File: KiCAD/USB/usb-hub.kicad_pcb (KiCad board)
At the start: 2 copper layers, 15 x 20 mm, 1 part, among them J1 046809610110846+ Male

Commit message: stuffs
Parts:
- added C1: 0.1μF, Capacitor_SMD:C_01005_0402Metric, F.Cu at (144.0, 42.5)
- added C10: 30 pF, Capacitor_SMD:C_01005_0402Metric, F.Cu at (149.2, 50.3)
- added C11: 30 pF, Capacitor_SMD:C_01005_0402Metric, F.Cu at (154.6, 45.4)
- added C2: 0.1μF, Capacitor_SMD:C_01005_0402Metric, F.Cu at (122.5, 41.5)
- added C3: 0.1μF, Capacitor_SMD:C_01005_0402Metric, F.Cu at (122.5, 43.2)
- added C4: 0.1μF, Capacitor_SMD:C_01005_0402Metric, F.Cu at (122.5, 44.8)
- added C5: 0.1μF, Capacitor_SMD:C_01005_0402Metric, F.Cu at (122.5, 46.5)
- added C6: 10μF, Capacitor_SMD:C_01005_0402Metric, F.Cu at (143.2, 38.5)
- added C8: 10μF, Capacitor_SMD:C_01005_0402Metric, F.Cu at (122.5, 48.1)
- added C9: 10μF, Capacitor_SMD:C_01005_0402Metric, F.Cu at (122.5, 49.8)
- added R1: 649Ω, Resistor_SMD:R_0402_1005Metric, F.Cu at (119.9, 41.7)
- added R2: 10kΩ, Resistor_SMD:R_0402_1005Metric, F.Cu at (151.3, 41.4)
- added R3: 10kΩ, Resistor_SMD:R_0402_1005Metric, F.Cu at (119.9, 43.7)
- added R4: 10kΩ, Resistor_SMD:R_0402_1005Metric, F.Cu at (119.9, 45.7)
- added R5: 10kΩ, Resistor_SMD:R_0402_1005Metric, F.Cu at (119.9, 47.7)
- added R6: 0Ω, Resistor_SMD:R_0402_1005Metric, F.Cu at (119.9, 49.7)
- added R7: 1kΩ, Resistor_SMD:R_0402_1005Metric, F.Cu at (119.9, 51.7)
- added U1: CY7C65634-28LTXC, footprints:QFN-28, F.Cu at (148.0, 44.0)
- added Y1: 12MHz 20pF, Crystal:Crystal_SMD_Abracon_ABM3B-4Pin_5.0x3.2mm, F.Cu at (151.9, 48.0)
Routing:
- net X_IN: track 0.00 -> 8.69 mm
- net X_OUT: track 0.00 -> 8.66 mm
- net GND: track 0.00 -> 5.71 mm, vias 0 -> 3
- net VREG: track 0.00 -> 2.92 mm, vias 0 -> 2
- net Net-(U1-*RESET): track 0.00 -> 1.30 mm
- added copper zone on In1.Cu, net GND
- added copper zone on In2.Cu, net VREG
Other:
- board size 15 x 20 mm -> 16 x 20 mm
- copper layers 2 -> 4

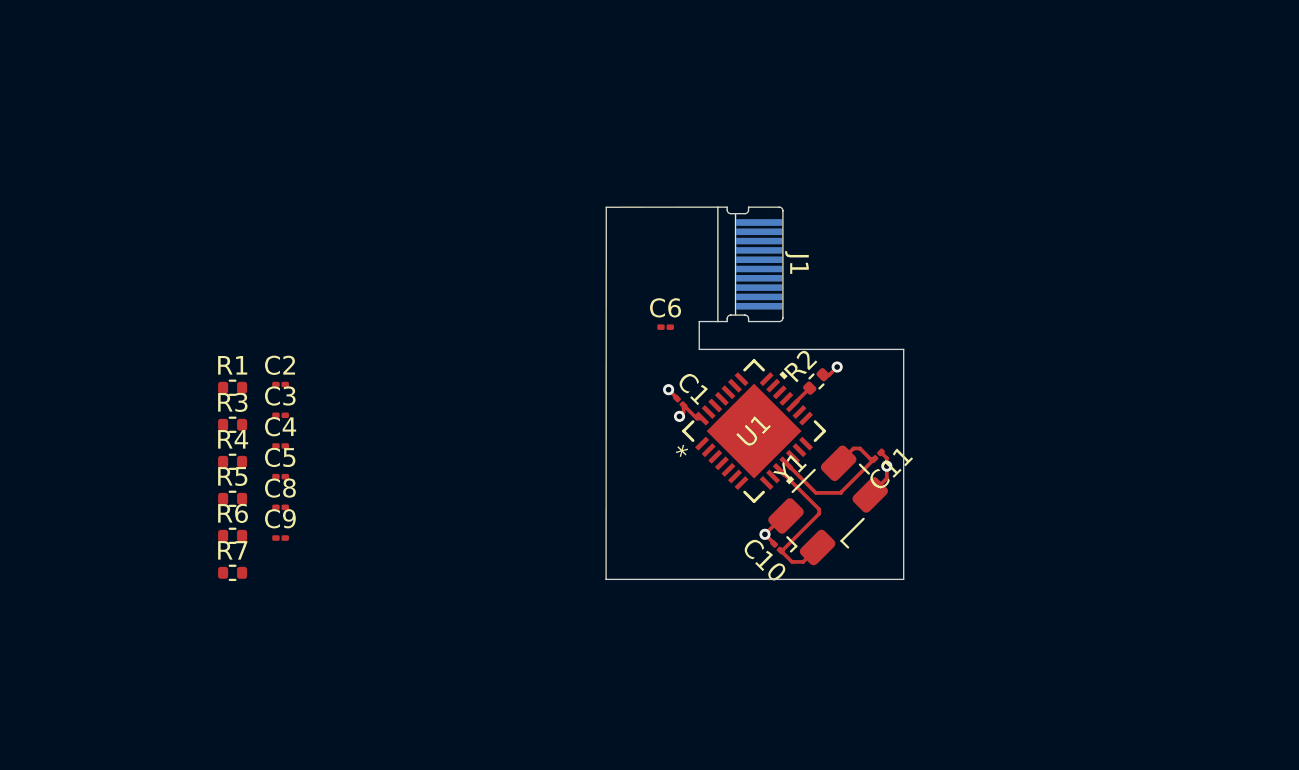
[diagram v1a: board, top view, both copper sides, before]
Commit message: Finish USB hub pcb
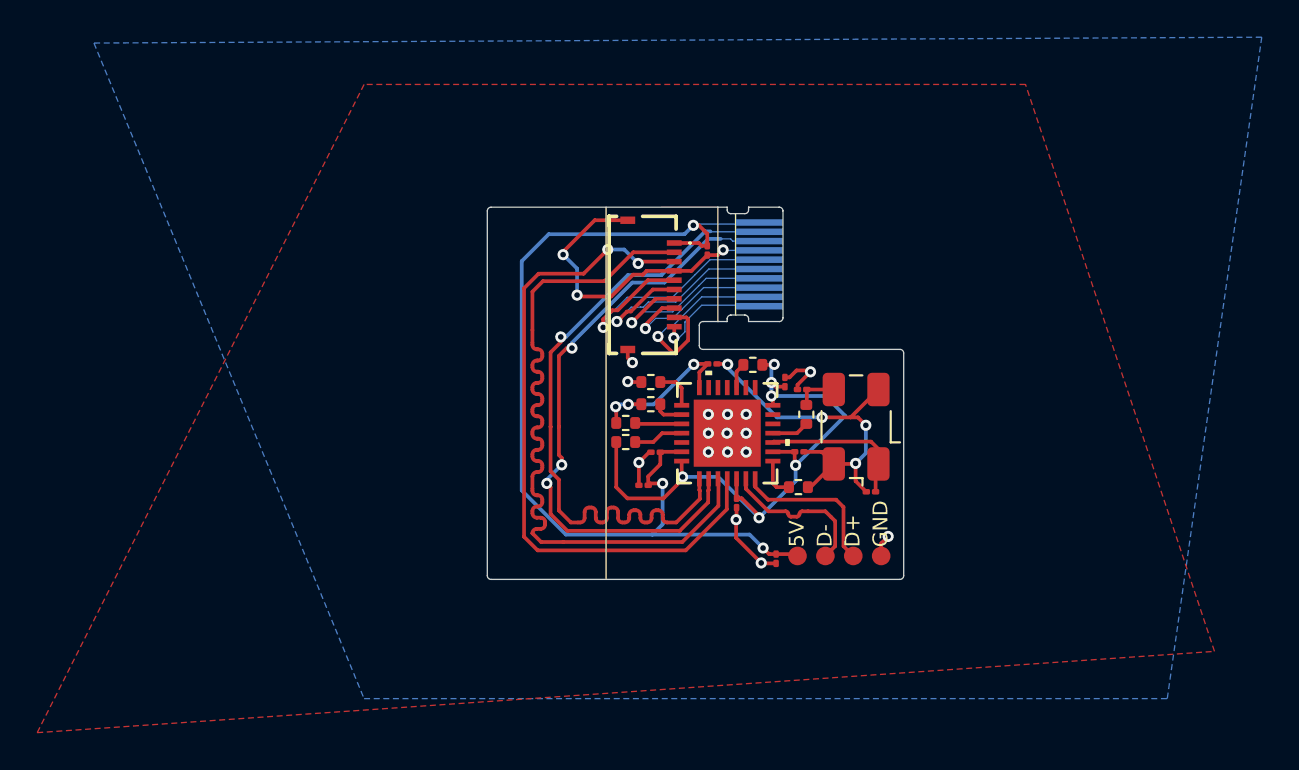
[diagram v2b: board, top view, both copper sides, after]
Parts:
- added J2: 046809610110846+ Female, SamacSys_Parts:046809610110846, F.Cu at (142.0, 36.2)
- added J3: Conn_01x04_Socket, Custom:4 pad, F.Cu at (152.6, 50.8)
- moved R7 32.0 mm to (150.8, 43.1), turned to 90 degrees
- moved R1 30.9 mm to (150.3, 47.0)
- moved C3 28.0 mm to (150.4, 45.1)
- moved C4 27.3 mm to (149.6, 41.4), turned to 90 degrees
- moved C8 26.8 mm to (145.4, 34.3), turned to 90 degrees
- moved C9 26.7 mm to (149.2, 50.9), turned to 90 degrees
- moved C2 25.3 mm to (147.0, 47.9), turned to -90 degrees
- moved R6 24.0 mm to (142.4, 41.4)
- moved R3 22.5 mm to (142.4, 42.6), turned to 180 degrees
- moved R5 21.5 mm to (141.1, 43.6)
- moved R4 21.2 mm to (141.1, 44.6), turned to 180 degrees
- moved C5 20.2 mm to (142.7, 45.2)
- moved C6 8.58 mm to (142.0, 47.0)
- moved C10 5.85 mm to (154.2, 47.3), turned to 180 degrees
- moved C11 5.40 mm to (150.6, 41.8), turned to 0 degrees
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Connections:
- U1 pad 3: USB_KB_N -> USB_FNG_N
- U1 pad 4: USB_KB_P -> USB_FNG_P
- U1 pad 6: USB_FNG_N -> USB_KB_N
- U1 pad 7: USB_FNG_P -> USB_KB_P
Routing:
- net VBUS: track 0.00 -> 52.7 mm, vias 0 -> 3
- net GND: track 5.71 -> 50.4 mm, vias 3 -> 23
- net USB_FNG_N: track 0.00 -> 39.2 mm
- net VREG: track 2.92 -> 41.9 mm, vias 2 -> 9
- net USB_FNG_P: track 0.00 -> 36.4 mm, vias 0 -> 2
- net USB_HOST_N: track 0.00 -> 36.3 mm, vias 0 -> 1
- net USB_HOST_P: track 0.00 -> 33.3 mm, vias 0 -> 3
- net EC_CTRL: track 0.00 -> 15.2 mm, vias 0 -> 1
- net SWITCH: track 0.00 -> 12.7 mm, vias 0 -> 1
- net RGB_W: track 0.00 -> 10.7 mm, vias 0 -> 1
- net RGB_R: track 0.00 -> 10.6 mm, vias 0 -> 1
- net RGB_G: track 0.00 -> 9.16 mm, vias 0 -> 1
- net USB_KB_N: track 0.00 -> 8.49 mm
- net USB_KB_P: track 0.00 -> 8.48 mm
- net X_OUT: track 8.66 -> 2.01 mm
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- added copper zone on B.Cu, net GND
- added copper zone on F.Cu, net VREG
- removed copper zone on In1.Cu, net GND
- removed copper zone on In2.Cu, net VREG
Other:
- board size 16 x 20 mm -> 22.4 x 20 mm
- copper layers 4 -> 2
- board text added: "5V"
- board text added: "D+"
- board text added: "D-"
- board text added: "GND"

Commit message: move stuff and fix constraints
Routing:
- net SWITCH: track 12.7 -> 14.4 mm
- net RGB_R: track 10.6 -> 8.98 mm
- net RGB_W: track 10.7 -> 11.9 mm
- net LED_COM: track 6.26 -> 7.03 mm

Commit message: production files + goldfinger
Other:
- board text added: "JLCJLCJLCJLC"

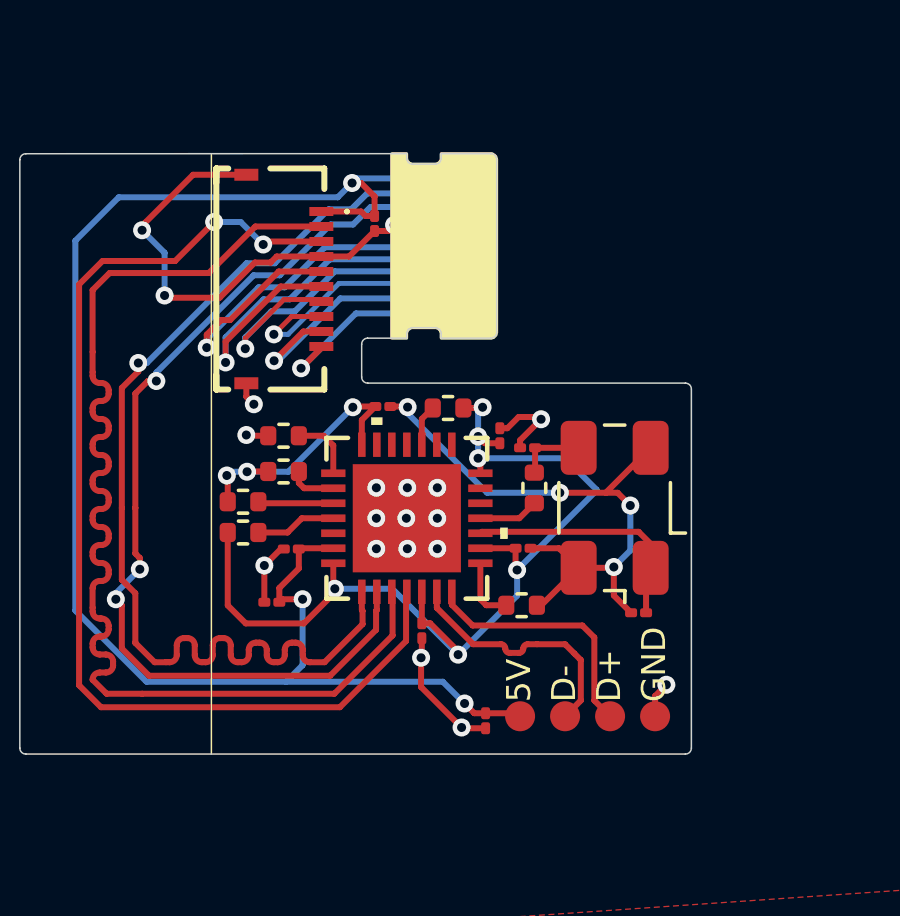
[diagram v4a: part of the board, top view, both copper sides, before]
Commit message: ofc i had to be using the wrong footprint
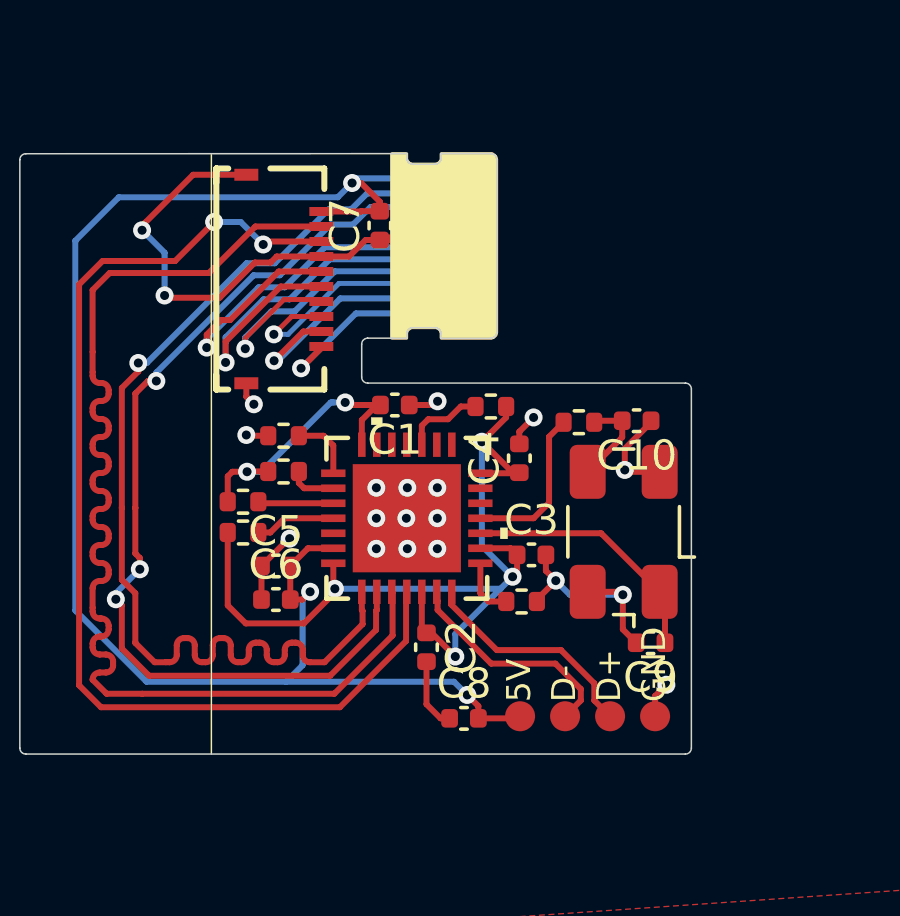
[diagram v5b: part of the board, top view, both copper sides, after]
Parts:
- C1, C2, C3, C4, C5, C6: footprint Capacitor_SMD:C_01005_0402Metric -> Capacitor_SMD:C_0402_1005Metric
- C10: renamed from C11; footprint Capacitor_SMD:C_01005_0402Metric -> Capacitor_SMD:C_0402_1005Metric
- C7: renamed from C8; footprint Capacitor_SMD:C_01005_0402Metric -> Capacitor_SMD:C_0402_1005Metric
- C8: renamed from C9; footprint Capacitor_SMD:C_01005_0402Metric -> Capacitor_SMD:C_0402_1005Metric
- C9: renamed from C10; footprint Capacitor_SMD:C_01005_0402Metric -> Capacitor_SMD:C_0402_1005Metric
- moved C10 3.74 mm to (154.2, 40.9), turned to 180 degrees
- moved R7 2.65 mm to (152.3, 41.0), turned to 0 degrees
- moved R2 1.43 mm to (149.3, 40.4)
- moved C9 1.08 mm to (154.7, 48.3)
- moved C4 0.99 mm to (150.3, 42.1)
- moved Y1 0.85 mm to (153.8, 44.6)
- moved C5 0.76 mm to (142.2, 45.7)
- moved C8 0.72 mm to (148.4, 50.8), turned to 0 degrees
- moved C2 0.57 mm to (147.2, 48.5)
- moved C1 0.40 mm to (146.1, 40.4)
- moved C3 0.36 mm to (150.7, 45.4)
- moved C7 0.19 mm to (145.6, 34.4)
- moved C6 0.16 mm to (142.2, 46.9)
- moved R1 0.12 mm to (150.3, 46.9)
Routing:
- net GND: track 50.4 -> 38.3 mm, vias 23 -> 21
- net X_OUT: track 2.01 -> 5.39 mm
- net VREG: track 41.9 -> 40.2 mm, vias 9 -> 6
- net Net-(U1-*RESET): track 1.38 -> 2.69 mm
- net USB_KB_N: track 8.49 -> 7.61 mm
- net USB_KB_P: track 8.48 -> 7.61 mm
- net Net-(C10-Pad2): track 2.29 -> 3.14 mm
- net VBUS: track 52.7 -> 53.4 mm

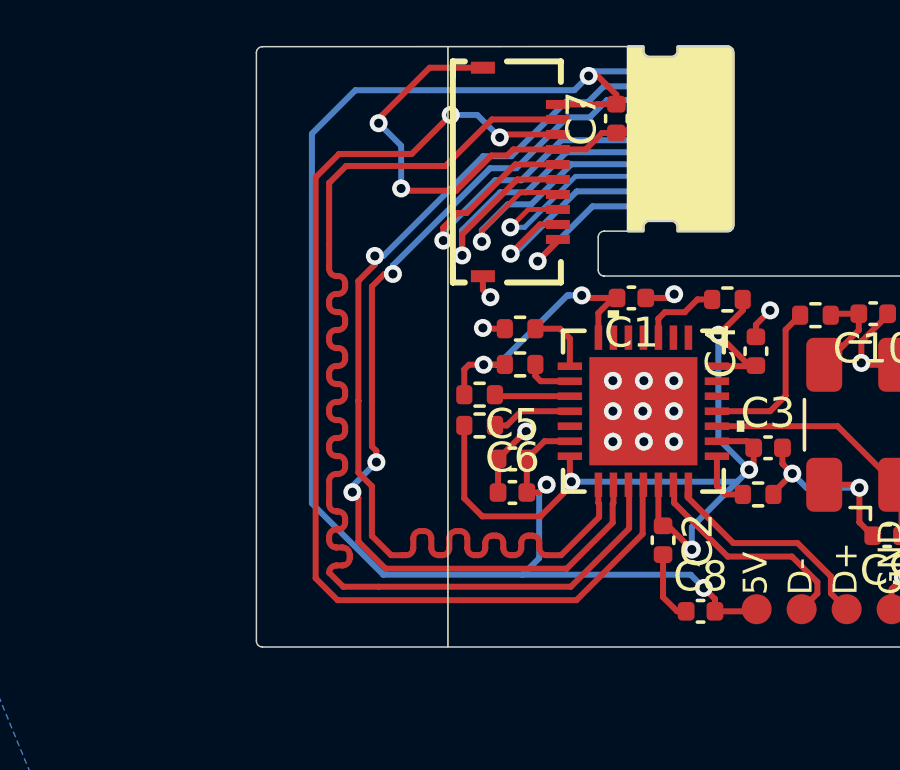
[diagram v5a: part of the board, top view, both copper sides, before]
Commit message: forgor to tune differential pair traces
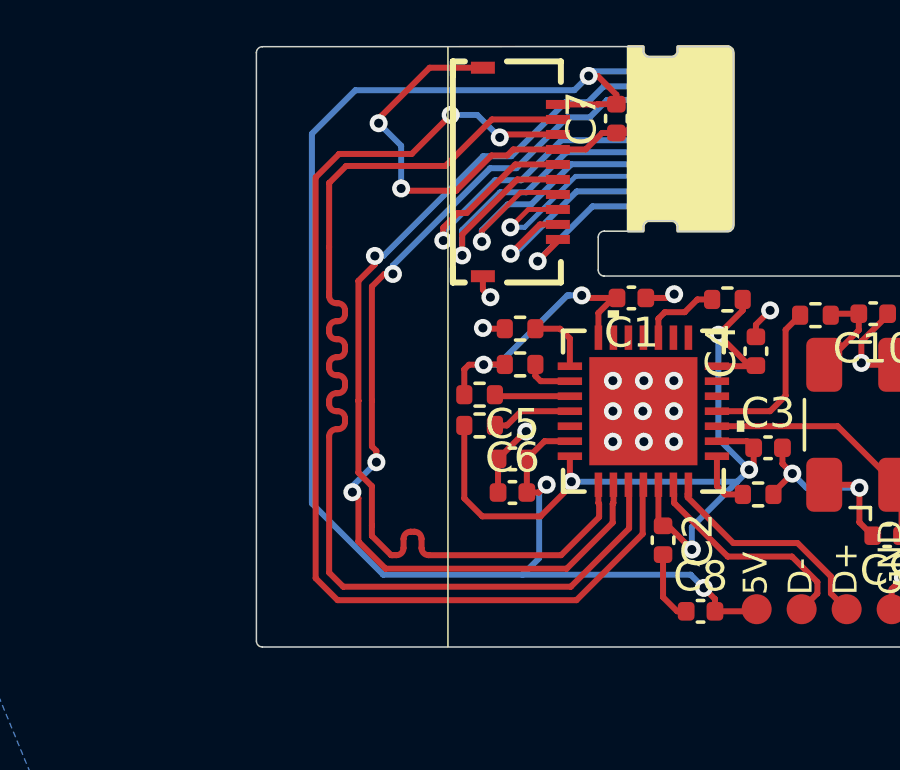
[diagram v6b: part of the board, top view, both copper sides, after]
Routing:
- net USB_HOST_N: track 36.2 -> 33.3 mm
- net USB_FNG_N: track 39.2 -> 36.4 mm

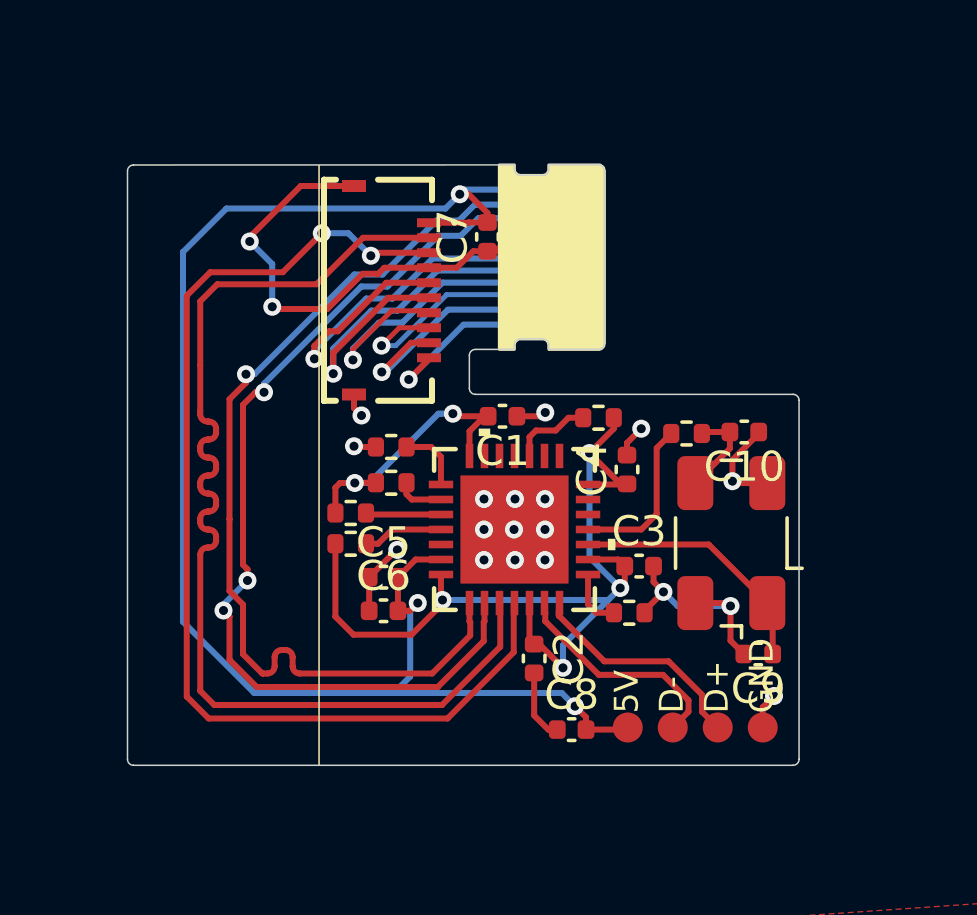
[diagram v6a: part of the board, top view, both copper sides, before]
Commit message: move vbus capacitor
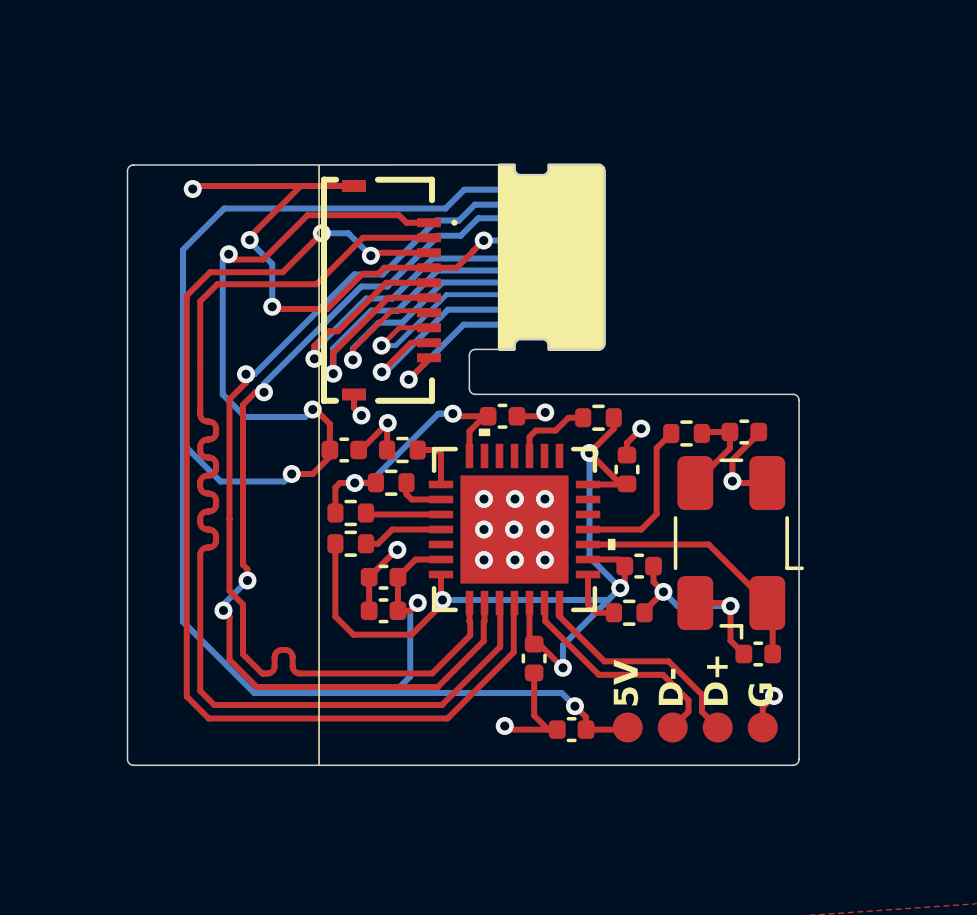
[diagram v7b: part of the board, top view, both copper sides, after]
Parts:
- moved C7 8.56 mm to (140.8, 41.5), turned to 180 degrees
- moved R6 0.39 mm to (142.8, 41.5)
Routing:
- net VBUS: track 53.4 -> 73.3 mm, vias 3 -> 5
- net GND: track 38.3 -> 45.3 mm, vias 21 -> 23
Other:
- board text added: "G"
- board text removed: "GND"
